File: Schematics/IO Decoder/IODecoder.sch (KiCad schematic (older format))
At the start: 2 parts, among them U2 74HCT138

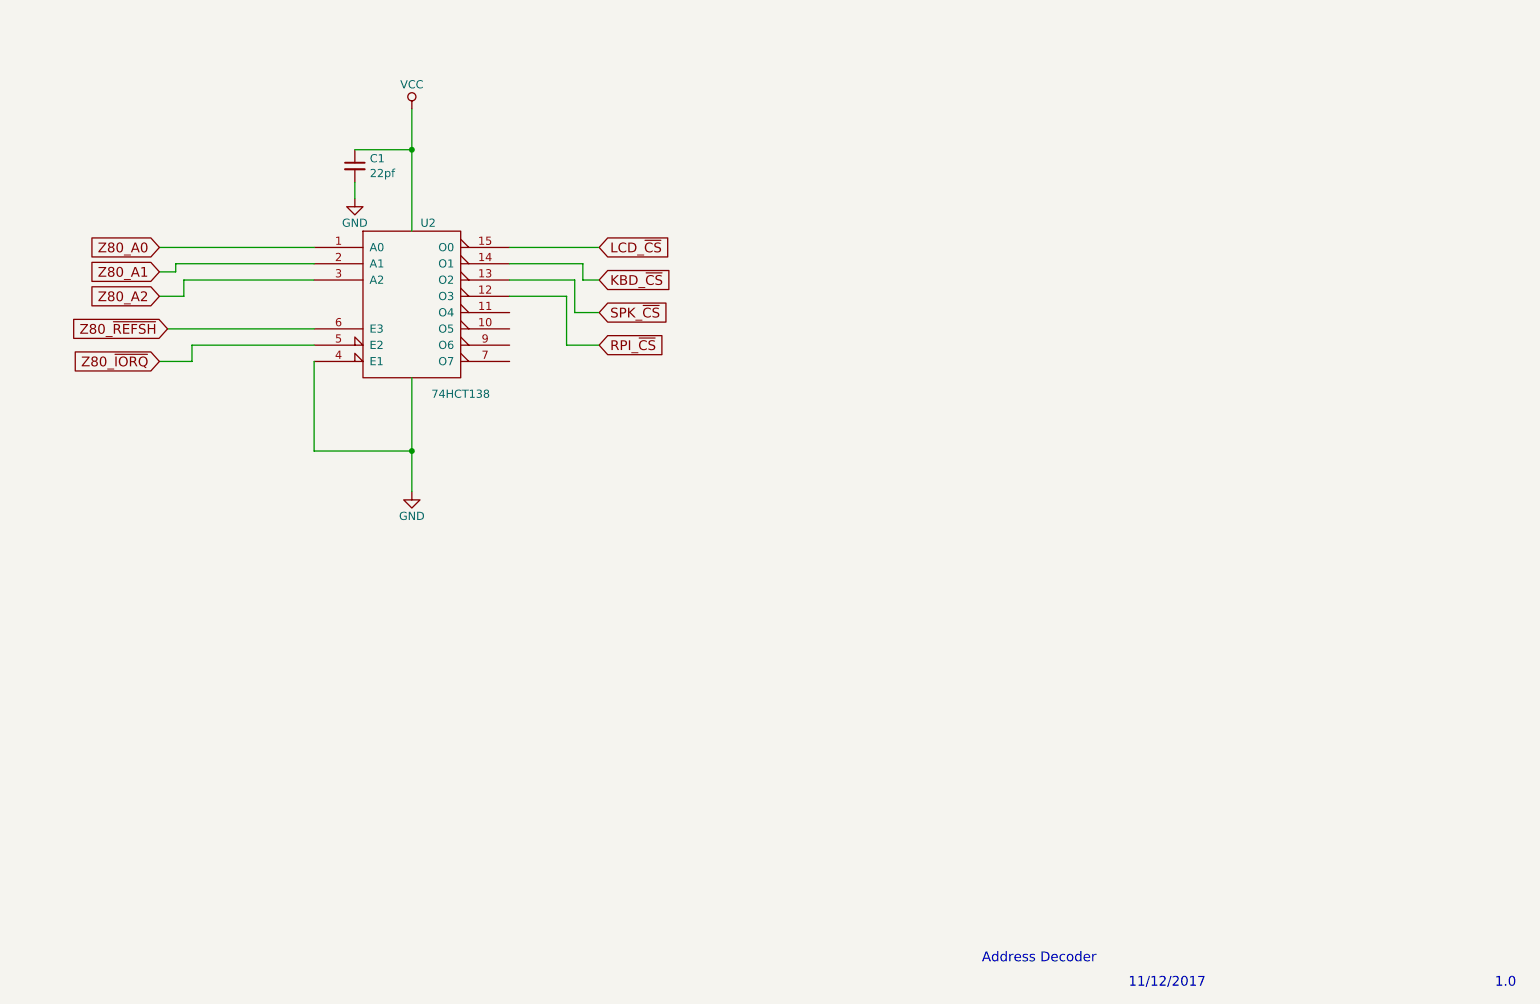
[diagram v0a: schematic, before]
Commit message: Minor changes in IO Decoder schematic
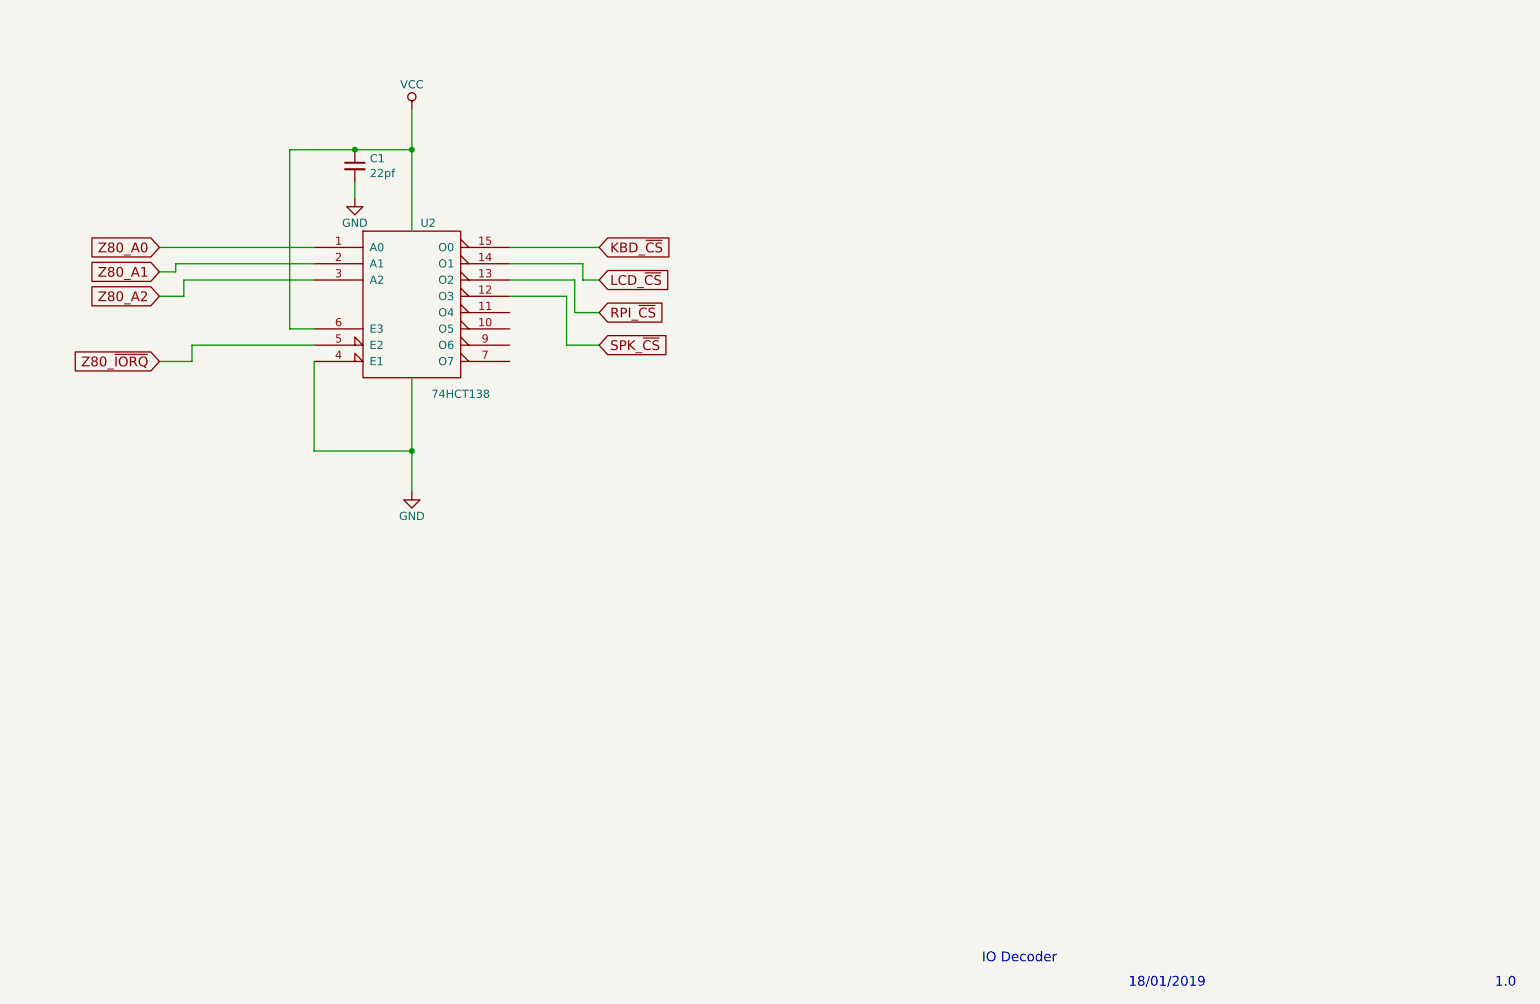
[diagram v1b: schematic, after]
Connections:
- net Z80_~REFSH is gone; now on net VCC: U2.6 (E3)
- net KBD_~CS: now also U2.15 (O0); no longer U2.14 (O1)
- net LCD_~CS: now also U2.14 (O1); no longer U2.15 (O0)
- net RPI_~CS: now also U2.13 (O2); no longer U2.12 (O3)
- net SPK_~CS: now also U2.12 (O3); no longer U2.13 (O2)
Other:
- note added: "18/01/2019"
- note added: "IO Decoder"
- note removed: "11/12/2017"
- note removed: "Address Decoder"
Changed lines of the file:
@@
 $EndComp
 Text Notes 7450 7500 0    60   ~ 0
-Address Decoder
+IO Decoder
 Text Notes 8350 7650 0    60   ~ 0
-11/12/2017
+18/01/2019
 Text Notes 10600 7650 0    60   ~ 0
 1.0
@@
 	1    0    0    -1
 $EndComp
-Text GLabel 2450 3600 0    60   Input ~ 0
-Z80_~REFSH
 Wire Wire Line
 	3950 4350 3950 4600
@@
 	2600 3800 2400 3800
 Wire Wire Line
-	2450 3600 3350 3600
-Wire Wire Line
 	2400 3250 2500 3250
 Wire Wire Line
@@
 Wire Wire Line
 	2550 3300 3350 3300
-Text GLabel 5100 3100 2    60   Input ~ 0
+Text GLabel 5100 3300 2    60   Input ~ 0
 LCD_~CS
 Wire Wire Line
 	4550 3100 5100 3100
-Text GLabel 5100 3300 2    60   Input ~ 0
+Text GLabel 5100 3100 2    60   Input ~ 0
 KBD_~CS
+Text GLabel 5100 3700 2    60   Input ~ 0
+SPK_~CS
 Text GLabel 5100 3500 2    60   Input ~ 0
-SPK_~CS
-Text GLabel 5100 3700 2    60   Input ~ 0
 RPI_~CS
 Wire Wire Line
@@
 Wire Wire Line
 	3600 2700 3600 2800
+Wire Wire Line
+	3350 3600 3200 3600
+Wire Wire Line
+	3200 3600 3200 2500
+Wire Wire Line
+	3200 2500 3600 2500
+Connection ~ 3600 2500
 $EndSCHEMATC

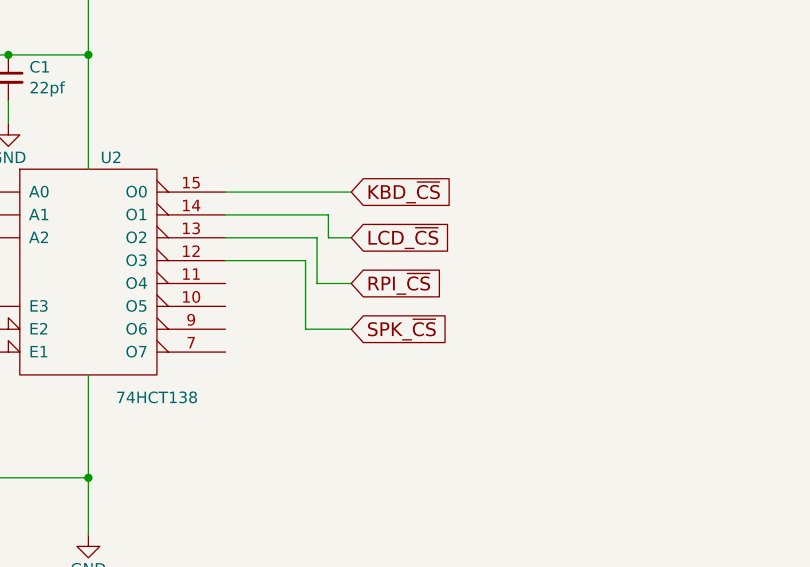
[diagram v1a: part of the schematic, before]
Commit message: Move IO Decoder to schematics and add Speaker and Joystick Ports
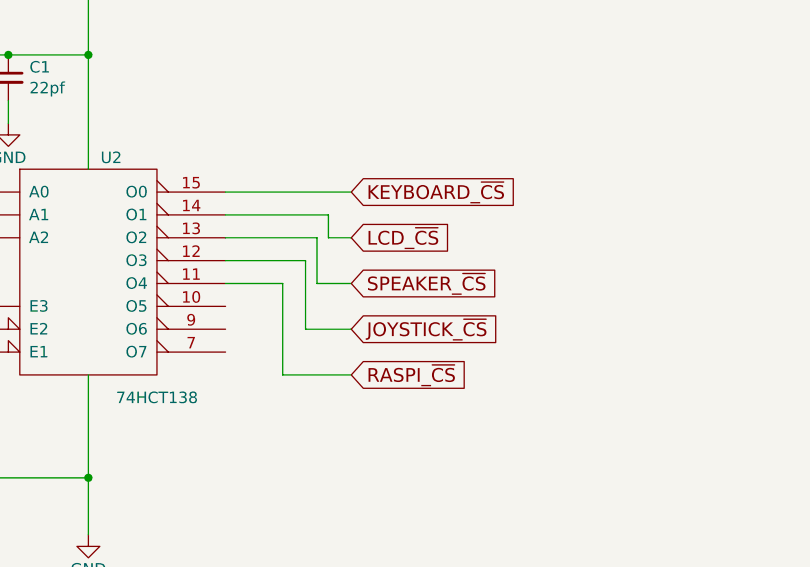
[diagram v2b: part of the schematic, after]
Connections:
- net RASPI_~CS: now reaches U2.11 (O4)
- net KBD_~CS renamed KEYBOARD_~CS
- net RPI_~CS renamed SPEAKER_~CS
- net SPK_~CS renamed JOYSTICK_~CS
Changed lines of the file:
@@
 	4550 3100 5100 3100
 Text GLabel 5100 3100 2    60   Input ~ 0
-KBD_~CS
+KEYBOARD_~CS
 Text GLabel 5100 3700 2    60   Input ~ 0
-SPK_~CS
+JOYSTICK_~CS
 Text GLabel 5100 3500 2    60   Input ~ 0
-RPI_~CS
+SPEAKER_~CS
 Wire Wire Line
 	4550 3200 5000 3200
@@
 	3200 2500 3600 2500
 Connection ~ 3600 2500
+Text GLabel 5100 3900 2    60   Input ~ 0
+RASPI_~CS
+Wire Wire Line
+	5100 3900 4800 3900
+Wire Wire Line
+	4800 3900 4800 3500
+Wire Wire Line
+	4800 3500 4550 3500
 $EndSCHEMATC

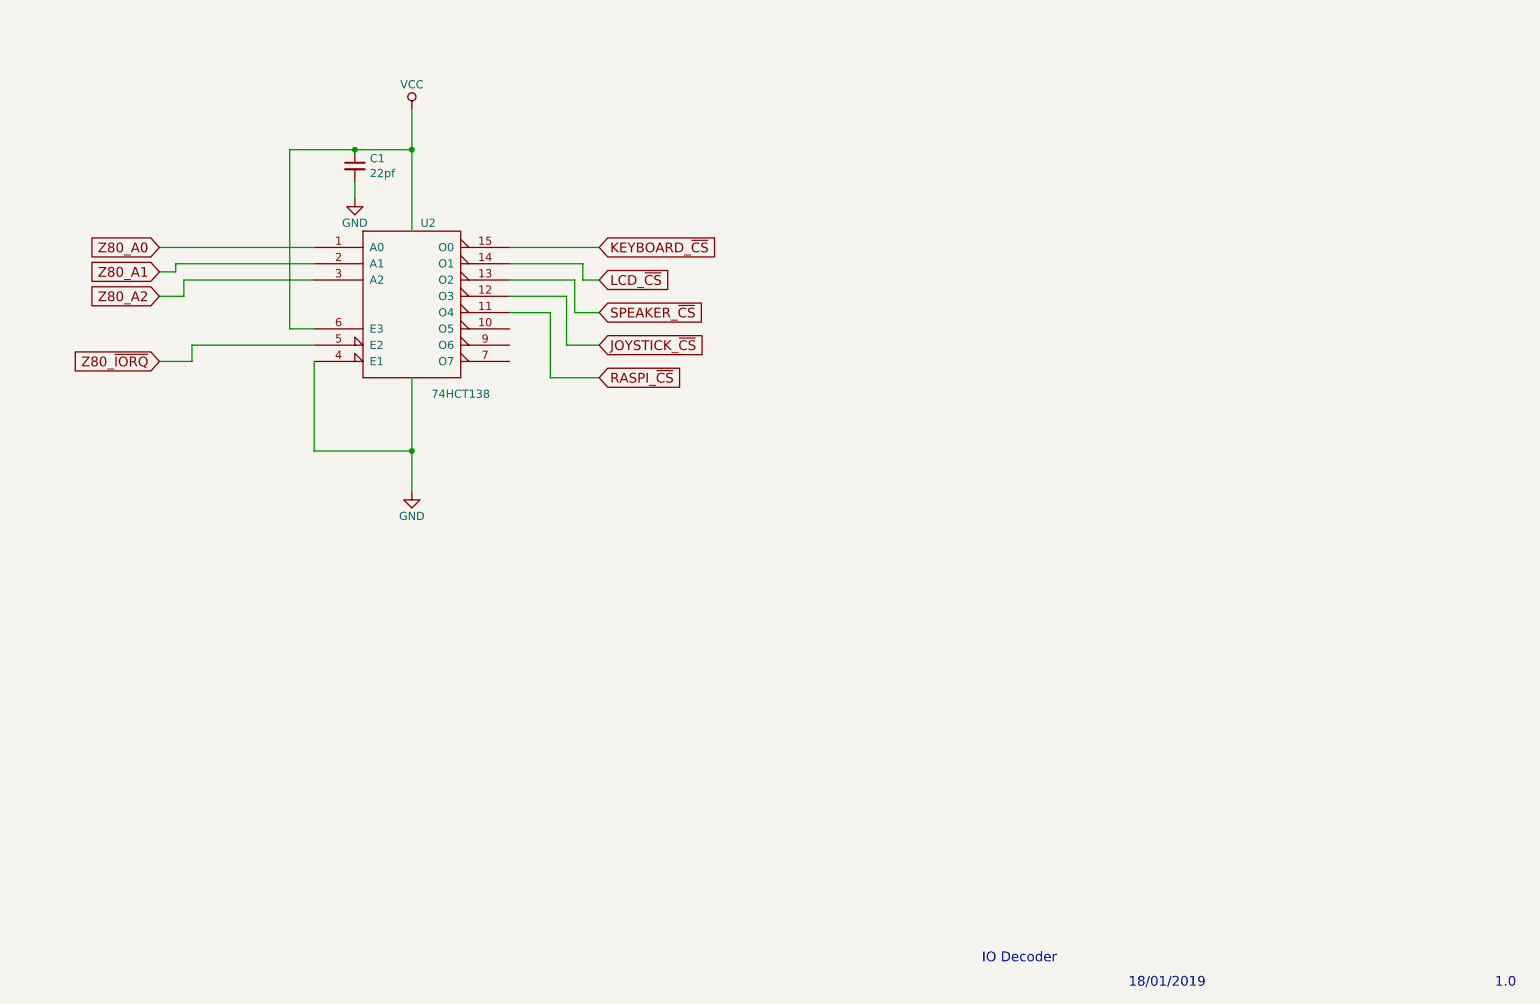
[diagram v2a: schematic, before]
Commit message: Redesign IO Decoder to include backplane
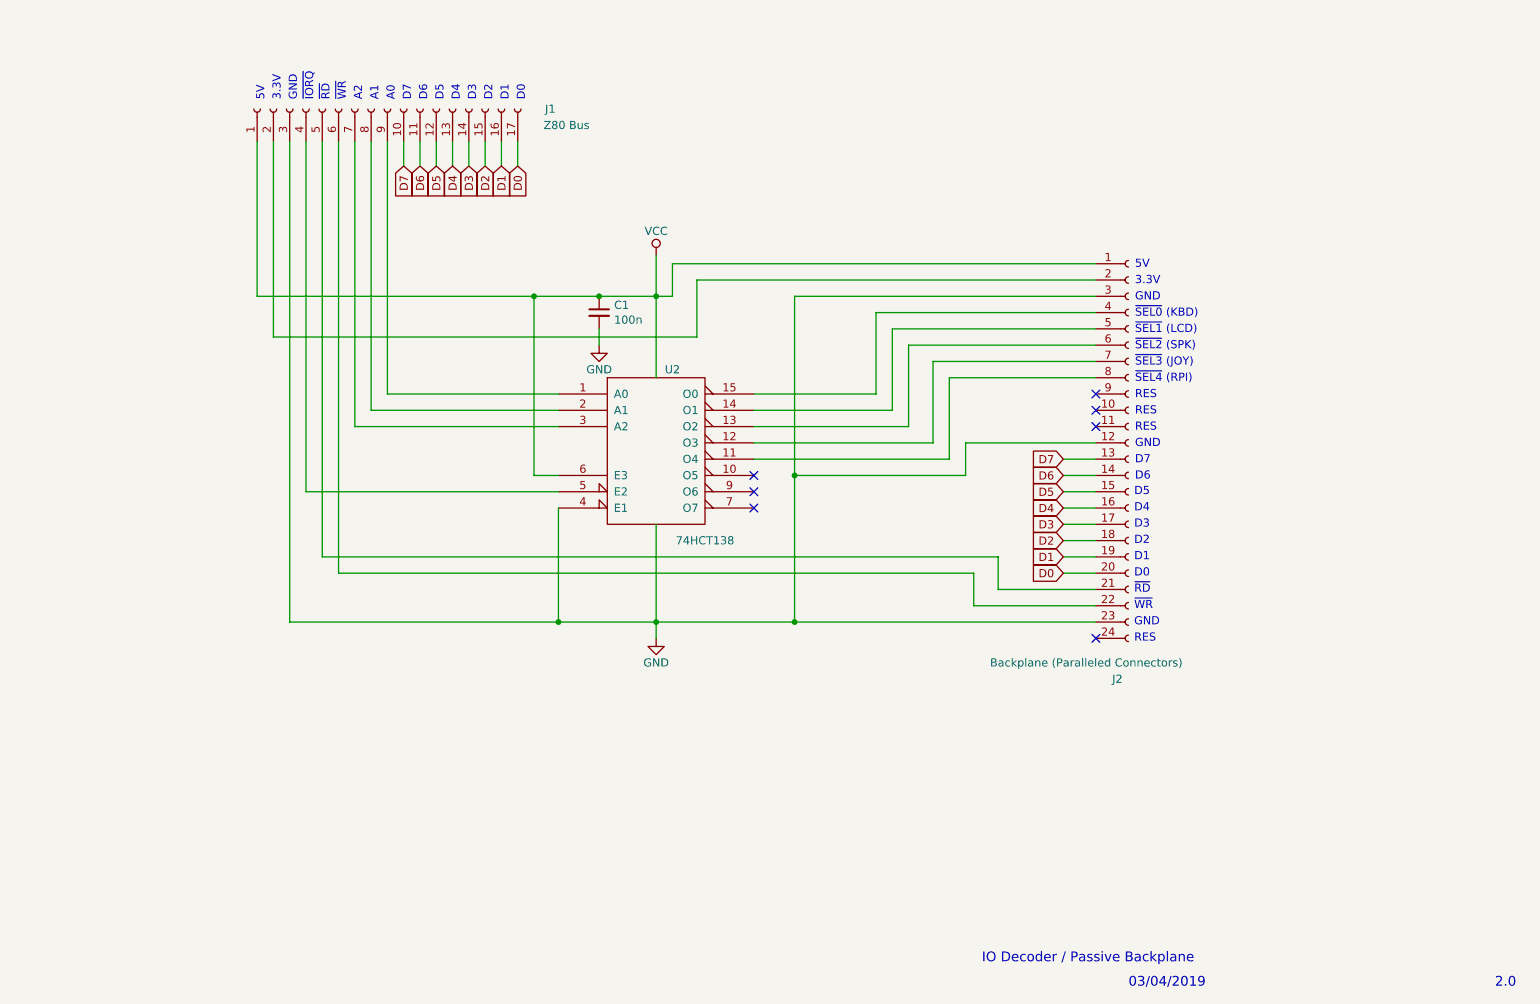
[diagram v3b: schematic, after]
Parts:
- added J1: Z80 Bus, symbol Connector:Conn_01x17_Female
- added J2: Backplane (Paralleled Connectors), symbol Connector:Conn_01x24_Female
- C1: value 22pf -> 100n
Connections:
- net GND: now also J1.3 (Pin_3), J2.12 (Pin_12), J2.23 (Pin_23), J2.3 (Pin_3)
- net VCC: now also J1.1 (Pin_1), J2.1 (Pin_1)
- net JOYSTICK_~CS: no longer names the net of U2.12 (O3)
- net JOYSTICK_~CS: now also J2.7 (Pin_7)
- net KEYBOARD_~CS: no longer names the net of U2.15 (O0)
- net KEYBOARD_~CS: now also J2.4 (Pin_4)
- net LCD_~CS: no longer names the net of U2.14 (O1)
- net LCD_~CS: now also J2.5 (Pin_5)
- net RASPI_~CS: no longer names the net of U2.11 (O4)
- net RASPI_~CS: now also J2.8 (Pin_8)
- net SPEAKER_~CS: no longer names the net of U2.13 (O2)
- net SPEAKER_~CS: now also J2.6 (Pin_6)
- net Z80_A0: no longer names the net of U2.1 (A0)
- net Z80_A0: now also J1.9 (Pin_9)
- net Z80_A1: no longer names the net of U2.2 (A1)
- net Z80_A1: now also J1.8 (Pin_8)
- net Z80_A2: no longer names the net of U2.3 (A2)
- net Z80_A2: now also J1.7 (Pin_7)
- net Z80_~ΙΟRQ: no longer names the net of U2.5 (E2)
- net Z80_~ΙΟRQ: now also J1.4 (Pin_4)
- new net: J1.2 (Pin_2), J2.2 (Pin_2)
- new net: J1.5 (Pin_5), J2.21 (Pin_21)
- new net: J1.6 (Pin_6), J2.22 (Pin_22)
- new net D0: J1.17 (Pin_17), J2.20 (Pin_20)
- new net D1: J1.16 (Pin_16), J2.19 (Pin_19)
- new net D2: J1.15 (Pin_15), J2.18 (Pin_18)
- new net D3: J1.14 (Pin_14), J2.17 (Pin_17)
- new net D4: J1.13 (Pin_13), J2.16 (Pin_16)
- new net D5: J1.12 (Pin_12), J2.15 (Pin_15)
- new net D6: J1.11 (Pin_11), J2.14 (Pin_14)
- new net D7: J1.10 (Pin_10), J2.13 (Pin_13)
- no-connect marks 0 -> 7
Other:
- note added: "03/04/2019"
- note added: "2.0"
- note added: "3.3V"
- note added: "5V"
- note added: "A0"
- note added: "A1"
- note added: "A2"
- note added: "D0"
- note added: "D1"
- note added: "D2"
- note added: "D3"
- note added: "D4"
- note added: "D5"
- note added: "D6"
- note added: "D7"
- note added: "GND"
- note added: "IO Decoder / Passive Backplane"
- note added: "RES"
- note added: "~IORQ"
- note added: "~RD"
- note added: "~SEL0 (KBD)"
- note added: "~SEL1 (LCD)"
- note added: "~SEL2 (SPK)"
- note added: "~SEL3 (JOY)"
- note added: "~SEL4 (RPI)"
- note added: "~WR"
- note removed: "1.0"
- note removed: "18/01/2019"
- note removed: "IO Decoder"
- moved on the sheet: C1, U2

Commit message: Change connector layouts of IO Decoder to match existing Display port layout on main board
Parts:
- added J2: Secondary Connector - Left to Right, symbol Connector:Conn_01x05_Female
- J1: value Z80 Bus -> Z80 Bus (Display port) - Left to Right; symbol Connector:Conn_01x17_Female -> Connector:Conn_01x12_Female
- renumbered J2 to J3
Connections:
- wire segments 77 -> 78
- no-connect marks 7 -> 1
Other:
- note added: "2.1"
- note added: "IO Decoder / System Backplane"
- note removed: "2.0"
- note removed: "IO Decoder / Passive Backplane"
- moved on the sheet: C1, J3
